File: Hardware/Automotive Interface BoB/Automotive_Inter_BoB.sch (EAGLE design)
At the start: 31 parts, among them U1 HCPL-270L

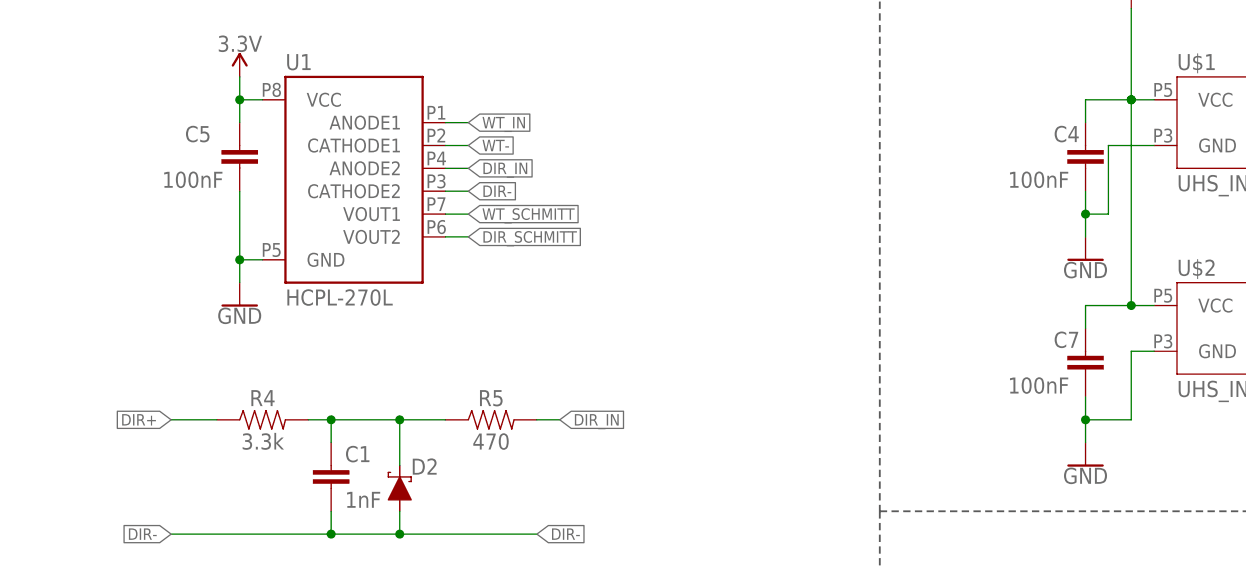
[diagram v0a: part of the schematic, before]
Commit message: CAMs the Automotive Interface Board, updates parts in library with digikey links
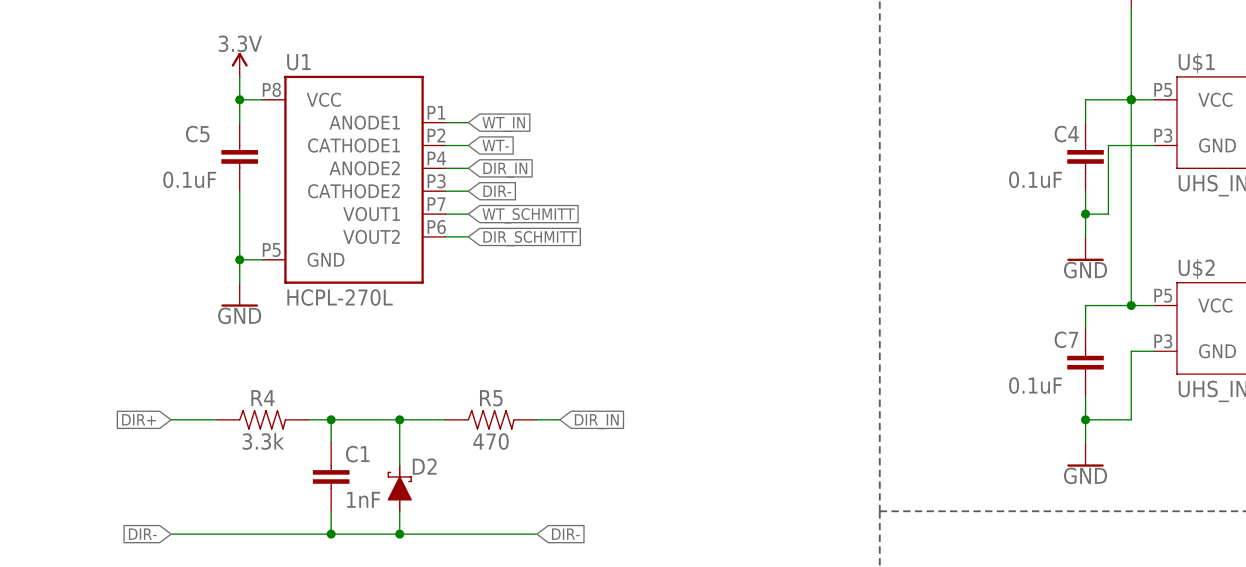
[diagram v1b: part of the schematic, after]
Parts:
- C4, C5, C7: value 100nF -> 0.1uF; device classified:100NF-0603-10V-10% -> SparkFun-Capacitors:0.1UF-0603-100V-10%
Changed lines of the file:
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@@
 <part name="R6" library="classified" deviceset="910OHM-0603-1/10W-5%" device="" value="910"/>
 <part name="U1" library="classified" deviceset="HCPL-270L" device=""/>
-<part name="C5" library="classified" deviceset="100NF-0603-10V-10%" device="" value="100nF"/>
+<part name="C5" library="SparkFun-Capacitors" deviceset="0.1UF" device="-0603-100V-10%" value="0.1uF"/>
 <part name="SUPPLY1" library="SparkFun-PowerSymbols" deviceset="3.3V" device=""/>
 <part name="GND1" library="SparkFun-PowerSymbols" deviceset="GND" device=""/>
@@
 <part name="H3" library="SparkFun-Hardware" deviceset="STAND-OFF" device=""/>
 <part name="H4" library="SparkFun-Hardware" deviceset="STAND-OFF" device=""/>
-<part name="C4" library="classified" deviceset="100NF-0603-10V-10%" device="" value="100nF"/>
-<part name="C7" library="classified" deviceset="100NF-0603-10V-10%" device="" value="100nF"/>
+<part name="C4" library="SparkFun-Capacitors" deviceset="0.1UF" device="-0603-100V-10%" value="0.1uF"/>
+<part name="C7" library="SparkFun-Capacitors" deviceset="0.1UF" device="-0603-100V-10%" value="0.1uF"/>
 <part name="LOGO1" library="SparkFun-Aesthetics" deviceset="SFE_LOGO_NAME_FLAME" device=".1_INCH" value="SFE_LOGO_NAME_FLAME.1_INCH"/>
 <part name="LOGO2" library="SparkFun-Aesthetics" deviceset="OSHW-LOGO" device="S" value="OSHW-LOGOS"/>

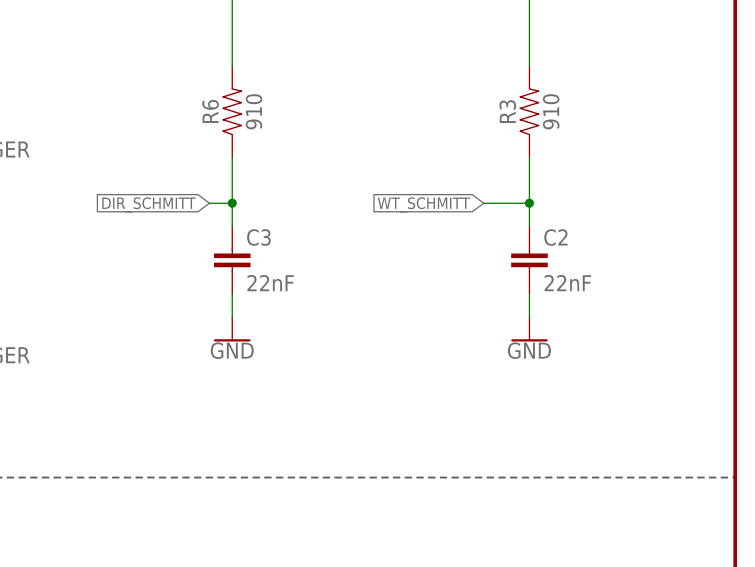
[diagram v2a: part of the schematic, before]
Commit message: Updates wheel tick and direction circuitry with correct grounding
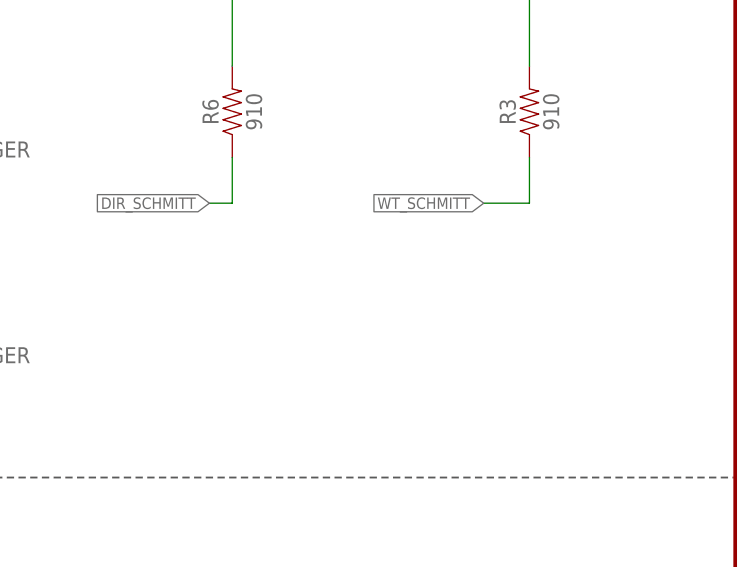
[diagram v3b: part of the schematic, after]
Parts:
- removed C2, C3: 22nF, SparkFun-Capacitors:22NF/22,000PF-0603-50V-10%
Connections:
- net DIR_SCHMITT: no longer C3.1
- net GND: no longer C2.2, C3.2
- net WT_SCHMITT: no longer C2.1
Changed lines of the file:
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@@
 <part name="R5" library="SparkFun-Resistors" deviceset="470OHM" device="-0603-1/10W-1%" value="470"/>
 <part name="C1" library="SparkFun-Capacitors" deviceset="1.0NF/1000PF" device="-0603-50V-10%" value="1nF"/>
-<part name="C2" library="SparkFun-Capacitors" deviceset="22NF/22,000PF" device="-0603-50V-10%" value="22nF"/>
-<part name="C3" library="SparkFun-Capacitors" deviceset="22NF/22,000PF" device="-0603-50V-10%" value="22nF"/>
 <part name="C6" library="SparkFun-Capacitors" deviceset="1.0NF/1000PF" device="-0603-50V-10%" value="1nF"/>
 <part name="D1" library="SparkFun-DiscreteSemi" deviceset="DIODE-SCHOTTKY" device="-PMEG4005EJ" value="0.5A/40V/420mV"/>
@@
 <part name="GND2" library="SparkFun-PowerSymbols" deviceset="GND" device=""/>
 <part name="D2" library="SparkFun-DiscreteSemi" deviceset="DIODE-SCHOTTKY" device="-PMEG4005EJ" value="0.5A/40V/420mV"/>
-<part name="GND4" library="SparkFun-PowerSymbols" deviceset="GND" device=""/>
-<part name="GND3" library="SparkFun-PowerSymbols" deviceset="GND" device=""/>
 <part name="SUPPLY4" library="SparkFun-PowerSymbols" deviceset="3.3V" device=""/>
 <part name="SUPPLY5" library="SparkFun-PowerSymbols" deviceset="3.3V" device=""/>
@@
 <attribute name="VALUE" x="39.624" y="107.061" size="1.778" layer="96" font="vector"/>
 </instance>
-<instance part="C2" gate="G$1" x="226.06" y="129.54" smashed="yes">
-<attribute name="NAME" x="227.584" y="132.461" size="1.778" layer="95" font="vector"/>
-<attribute name="VALUE" x="227.584" y="127.381" size="1.778" layer="96" font="vector"/>
-</instance>
-<instance part="C3" gate="G$1" x="193.04" y="129.54" smashed="yes">
-<attribute name="NAME" x="194.564" y="132.461" size="1.778" layer="95" font="vector"/>
-<attribute name="VALUE" x="194.564" y="127.381" size="1.778" layer="96" font="vector"/>
-</instance>
 <instance part="C6" gate="G$1" x="38.1" y="83.82" smashed="yes">
 <attribute name="NAME" x="39.624" y="86.741" size="1.778" layer="95" font="vector"/>
@@
 <instance part="D2" gate="G$1" x="45.72" y="109.22" smashed="yes" rot="R90">
 <attribute name="NAME" x="50.038" y="112.522" size="1.778" layer="95" font="vector" rot="R180"/>
-</instance>
-<instance part="GND4" gate="1" x="193.04" y="121.92" smashed="yes">
-<attribute name="VALUE" x="193.04" y="121.666" size="1.778" layer="96" align="top-center"/>
-</instance>
-<instance part="GND3" gate="1" x="226.06" y="121.92" smashed="yes">
-<attribute name="VALUE" x="226.06" y="121.666" size="1.778" layer="96" align="top-center"/>
 </instance>
 <instance part="SUPPLY4" gate="G$1" x="226.06" y="160.02" smashed="yes">
@@
 </segment>
 <segment>
-<pinref part="C2" gate="G$1" pin="2"/>
-<pinref part="GND3" gate="1" pin="GND"/>
-<wire x1="226.06" y1="124.46" x2="226.06" y2="127" width="0.1524" layer="91"/>
-</segment>
-<segment>
-<pinref part="C3" gate="G$1" pin="2"/>
-<pinref part="GND4" gate="1" pin="GND"/>
-<wire x1="193.04" y1="127" x2="193.04" y2="124.46" width="0.1524" layer="91"/>
-</segment>
-<segment>
 <pinref part="J1" gate="G$1" pin="1"/>
 <wire x1="35.56" y1="12.7" x2="38.1" y2="12.7" width="0.1524" layer="91"/>
@@
 <pinref part="R3" gate="G$1" pin="1"/>
 <wire x1="226.06" y1="142.24" x2="226.06" y2="137.16" width="0.1524" layer="91"/>
-<pinref part="C2" gate="G$1" pin="1"/>
-<wire x1="226.06" y1="137.16" x2="226.06" y2="134.62" width="0.1524" layer="91"/>
-<junction x="226.06" y="137.16"/>
 <label x="220.98" y="137.16" size="1.27" layer="95" font="vector" rot="R180" xref="yes"/>
 </segment>
@@
 <segment>
 <pinref part="R6" gate="G$1" pin="1"/>
-<pinref part="C3" gate="G$1" pin="1"/>
 <wire x1="193.04" y1="142.24" x2="193.04" y2="137.16" width="0.1524" layer="91"/>
-<wire x1="193.04" y1="137.16" x2="193.04" y2="134.62" width="0.1524" layer="91"/>
 <wire x1="193.04" y1="137.16" x2="190.5" y2="137.16" width="0.1524" layer="91"/>
-<junction x="193.04" y="137.16"/>
 <label x="190.5" y="137.16" size="1.27" layer="95" font="vector" rot="R180" xref="yes"/>
 </segment>
